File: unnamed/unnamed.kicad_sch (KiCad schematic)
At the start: 131 parts, among them J1 Serial, J2 Serial, J3 Conn_01x01_Female, J4 Conn_01x01_Female, J5 S3B-PH-SM4-TB(LF)(SN), J6 S3B-PH-SM4-TB(LF)(SN), J7 trackball, J8 Conn_01x12_Female, SW1 SW_Push, SW10 SW_Push, SW11 SW_Push, SW12 SW_Push, SW13 SW_Push, SW14 SW_Push, SW15 SW_Push, SW16 SW_Push, SW17 SW_Push, SW18 SW_Push, SW19 SW_Push, SW2 SW_Push, SW20 SW_Push, SW21 SW_Push, SW22 SW_Push, SW23 SW_Push, SW24 SW_Push, SW25 SW_SPST, SW26 SW_SPST, SW27 SW_Push, SW28 SW_Push, SW29 SW_Push, SW3 SW_Push, SW30 SW_Push, SW31 SW_Push, SW32 SW_Push, SW33 SW_Push, SW34 SW_Push, SW35 SW_Push, SW36 SW_Push, SW4 SW_Push, SW5 SW_Push, SW6 SW_Push, SW7 SW_Push, SW8 SW_Push, SW9 SW_Push, U1 eliteC, U2 eliteC

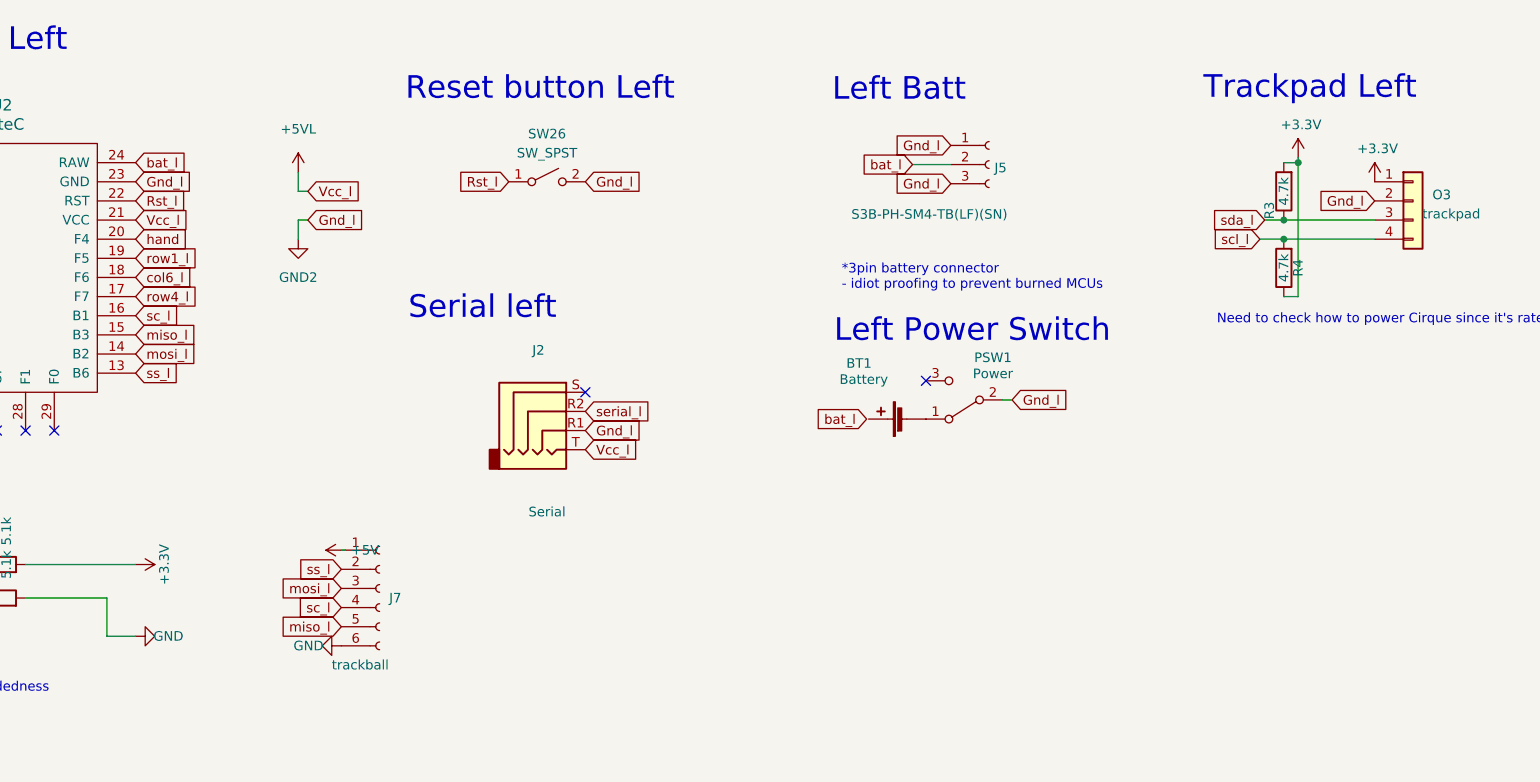
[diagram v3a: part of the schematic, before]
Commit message: trackpad connector
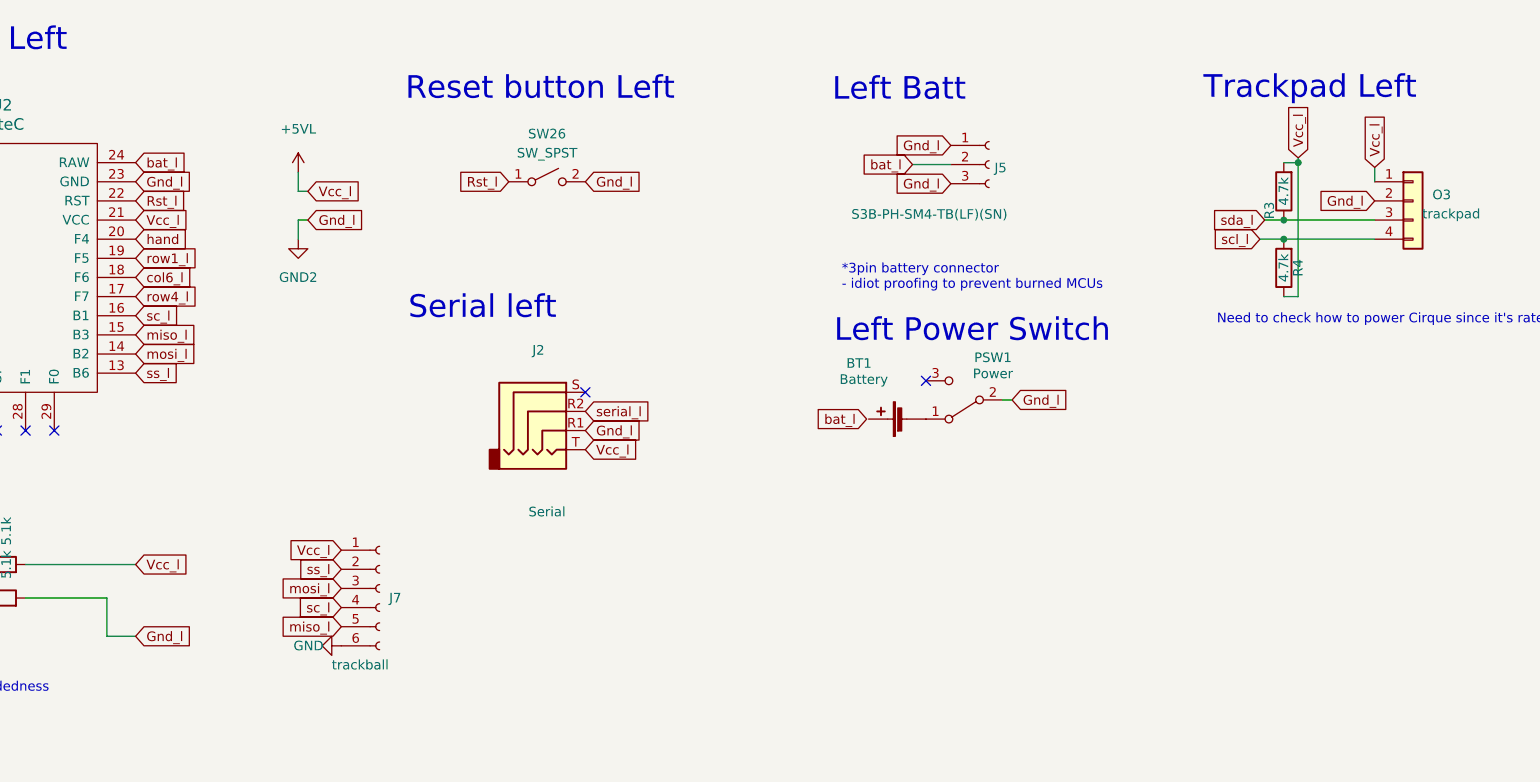
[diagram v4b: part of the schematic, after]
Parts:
- D10, D13, D14, D15, D18, D19, D20, D24, D25, D26, D3, D30, D33, D4, D5, D8, D9: footprint Library:D_1206_handsolder_reversible -> footprints:D_1206_handsolder_reversible
- O3: footprint Connector_PinHeader_2.54mm:PinHeader_1x04_P2.54mm_Vertical -> footprints:PinHeader_1x04_P2.54mm_Vertical
- R7, R8: footprint Resistor_SMD:R_0402_1005Metric -> footprints:D_1206_handsolder
- SW1, SW10, SW11, SW12, SW13, SW14, SW15, SW16, SW17, SW18, SW19, SW2, SW20, SW21, SW22, SW23, SW24, SW25, SW26, SW27, SW28, SW29, SW3, SW30, SW31, SW32, SW33, SW4, SW5, SW6, SW7, SW8, SW9: footprint Library:SW_MX_choc -> footprints:SW_MX_choc
- U2: footprint Library:Elite-C -> footprints:Elite-C
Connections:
- net +3V3: no longer O3.1 (Pin_1), R3.2, R4.1, R7.2
- net +5V: no longer J7.1 (Pin_1)
- net +5VL: now also J7.1 (Pin_1), O3.1 (Pin_1), R3.2, R4.1, R7.2
- net GND: no longer R8.2
- net GND2: now also R8.2

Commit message: cleanup (reversible)
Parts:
- removed BT2: Battery, swoop:Battery_pads_reversible, symbol Device:Battery_Cell
- removed C2: C, symbol Device:C
- removed D35, D36, D40, D41, D45, D46, D50, D51, D55, D56, D57, D61, D62, D63, D65, D66, D68: SK6812MINI, symbol LED:SK6812MINI
- removed D37, D38, D39, D42, D43, D44, D47, D48, D49, D52, D53, D54, D58, D59, D60, D64, D67: D, symbol Device:D
- removed J1: Serial, symbol Connector:AudioJack4
- removed J3: Conn_01x01_Female, symbol Connector:Conn_01x01_Female
- removed J6: S3B-PH-SM4-TB(LF)(SN), Connector_JST:JST_PH_S3B-PH-SM4-TB_1x03-1MP_P2.00mm_Horizontal, symbol Connector:Conn_01x03_Female
- removed J8: Conn_01x12_Female, prettylib:FPC-SMD_FH12-12S-0.5SH-55, symbol Connector:Conn_01x12_Female
- removed O1: OLED, swoop:OLED_jumpers, symbol Connector_Generic:Conn_01x04
- removed PSW2: Power, swoop:Power, symbol Switch:SW_SPDT
- removed R2: R, symbol Device:R
- removed R5, R6: 4.7k, reversible-kicad-footprints:R-0805_2012Metric, symbol Device:R
- removed SW18, SW19, SW20, SW21, SW22, SW23, SW24, SW27, SW28, SW29, SW30, SW31, SW32, SW33: SW_Push, footprints:SW_MX_choc, symbol Switch:SW_Push
- removed SW25: SW_SPST, footprints:SW_MX_choc, symbol Switch:SW_SPST
- removed SW34, SW35, SW36: SW_Push, symbol Switch:SW_Push
- removed U1: eliteC, symbol elite-C:eliteC
- added SW37: SW_SPST, Button_Switch_THT:SW_PUSH_6mm_H9.5mm, symbol Switch:SW_SPST
- J2: footprint (none) -> footprints:Jack_3.5mm_PJ320E_Horizontal_reversible
- SW26: footprint footprints:SW_MX_choc -> Button_Switch_SMD:SW_Push_1P1T_NO_6x6mm_H9.5mm
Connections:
- net col6_l is gone; now on net col5_l: D24.1 (K), D25.1 (K), D26.1 (K), U2.18 (F6)
- net GND2: now also SW37.2 (B)
- net Rst_l: now also SW37.1 (A)
- net col2_l: now also D10.1 (K), D8.1 (K), D9.1 (K), U2.12 (B5); no longer D3.1 (K), D30.1 (K), D4.1 (K), D5.1 (K), U2.11 (B4)
- net col3_l: now also D13.1 (K), D14.1 (K), D15.1 (K), D33.1 (K), U2.10 (E6); no longer D10.1 (K), D8.1 (K), D9.1 (K), U2.12 (B5)
- net col4_l: now also D18.1 (K), D19.1 (K), D20.1 (K), U2.9 (D7); no longer D13.1 (K), D14.1 (K), D15.1 (K), D33.1 (K), U2.10 (E6)
- net col5_l: no longer D18.1 (K), D19.1 (K), D20.1 (K), U2.9 (D7)
- new net col1_l: D3.1 (K), D30.1 (K), D4.1 (K), D5.1 (K), U2.11 (B4)
- no-connect marks 21 -> 7
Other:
- note removed: "MCU Right"
- note removed: "OLED Right"
- note removed: "Reset button Right"
- note removed: "Right"
- note removed: "Right Batt"
- note removed: "Serial right"
- note removed: "Trackpad Right"

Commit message: routing, audio jack, rst button
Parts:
- SW37: footprint Button_Switch_THT:SW_PUSH_6mm_H9.5mm -> Button_Switch_SMD:SW_Push_1P1T_NO_6x6mm_H9.5mm
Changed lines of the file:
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@@
     (property "Reference" "SW37" (id 0) (at 373.38 40.64 0))
     (property "Value" "SW_SPST" (id 1) (at 373.38 43.18 0))
-    (property "Footprint" "Button_Switch_THT:SW_PUSH_6mm_H9.5mm" (id 2) (at 373.38 46.99 0)
+    (property "Footprint" "Button_Switch_SMD:SW_Push_1P1T_NO_6x6mm_H9.5mm" (id 2) (at 373.38 46.99 0)
       (effects (font (size 1.27 1.27)) hide)
     )
@@
     )
     (path "/be3485fb-9d3c-40d5-abfd-0f4dfff6875d"
-      (reference "SW37") (unit 1) (value "SW_SPST") (footprint "Button_Switch_THT:SW_PUSH_6mm_H9.5mm")
+      (reference "SW37") (unit 1) (value "SW_SPST") (footprint "Button_Switch_SMD:SW_Push_1P1T_NO_6x6mm_H9.5mm")
     )
     (path "/be4a846f-e398-4560-93fc-42de85dc5e36"

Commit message: routing
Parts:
- R7, R8: footprint footprints:D_1206_handsolder -> footprints:R_1206_handsolder
- SW26, SW37: footprint Button_Switch_SMD:SW_Push_1P1T_NO_6x6mm_H9.5mm -> footprints:SW_Push_1P1T_NO_6x6mm_H9.5mm
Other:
- moved on the sheet: BT1, J2, J5, J7, O2, O3, PSW1, R3, R4, R7, R8, SW26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

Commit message: holes
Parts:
- added H1, H2, H3, H4: M4, footprints:MountingHole_3mm_Pad_thin, symbol Mechanical:MountingHole_Pad
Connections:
- net GND: now also H1.1, H2.1, H3.1, H4.1
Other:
- note added: "Plate screws"
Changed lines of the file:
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@@
+    (stroke (width 0) (type default) (color 0 0 0 0))
+  )
+  (polyline (pts (xy 315.595 24.13) (xy 315.595 48.895))
     (stroke (width 0) (type default) (color 0 0 0 0))
   )
@@
     (stroke (width 0) (type solid) (color 0 0 0 0))
   )
+  (polyline (pts (xy 288.925 24.13) (xy 315.595 24.13))
+    (stroke (width 0) (type default) (color 0 0 0 0))
+  )
   (wire (pts (xy 120.65 99.06) (xy 128.27 99.06))
     (stroke (width 0) (type solid) (color 0 0 0 0))
@@
     (stroke (width 0) (type default) (color 0 0 0 0))
   )
+  (polyline (pts (xy 315.595 48.895) (xy 288.925 48.895))
+    (stroke (width 0) (type default) (color 0 0 0 0))
+  )
   (wire (pts (xy 66.04 38.1) (xy 67.31 38.1))
+    (stroke (width 0) (type default) (color 0 0 0 0))
+  )
+  (polyline (pts (xy 288.925 24.13) (xy 288.925 48.895))
     (stroke (width 0) (type default) (color 0 0 0 0))
   )
@@
   (text "Handedness" (at 46.355 216.535 0)
     (effects (font (size 1.27 1.27)) (justify left bottom))
+  )
+  (text "Plate screws" (at 302.895 26.67 180)
+    (effects (font (size 1.27 1.27)) (justify right bottom))
   )
   (text "Left" (at 23.495 74.93 90)
@@
     (pin "2")
   )
+  (symbol (lib_id "Mechanical:MountingHole_Pad") (at 299.085 33.655 0) (unit 1)
+    (in_bom yes) (on_board yes)
+    (property "Reference" "H2" (id 0) (at 297.815 28.575 0)
+      (effects (font (size 1.27 1.27)) (justify left))
+    )
+    (property "Value" "M4" (id 1) (at 297.815 45.847 0)
+      (effects (font (size 1.27 1.27)) (justify left))
+    )
+    (property "Footprint" "footprints:MountingHole_3mm_Pad_thin" (id 2) (at 299.085 33.655 0)
+      (effects (font (size 1.27 1.27)) hide)
+    )
+    (property "Datasheet" "~" (id 3) (at 299.085 33.655 0)
+      (effects (font (size 1.27 1.27)) hide)
+    )
+    (pin "1")
+  )
+  (symbol (lib_id "Mechanical:MountingHole_Pad") (at 292.735 33.655 0) (unit 1)
+    (in_bom yes) (on_board yes)
+    (property "Reference" "H1" (id 0) (at 291.465 28.575 0)
+      (effects (font (size 1.27 1.27)) (justify left))
+    )
+    (property "Value" "M4" (id 1) (at 291.465 45.847 0)
+      (effects (font (size 1.27 1.27)) (justify left))
+    )
+    (property "Footprint" "footprints:MountingHole_3mm_Pad_thin" (id 2) (at 292.735 33.655 0)
+      (effects (font (size 1.27 1.27)) hide)
+    )
+    (property "Datasheet" "~" (id 3) (at 292.735 33.655 0)
+      (effects (font (size 1.27 1.27)) hide)
+    )
+    (pin "1")
+  )
   (symbol (lib_id "LED:SK6812MINI") (at 226.06 78.74 0) (unit 1)
     (in_bom yes) (on_board yes)
@@
     (pin "2")
   )
+  (symbol (lib_id "power:GND") (at 305.435 36.195 0) (unit 1)
+    (in_bom yes) (on_board yes)
+    (property "Reference" "#PWR0107" (id 0) (at 305.435 42.545 0)
+      (effects (font (size 1.27 1.27)) hide)
+    )
+    (property "Value" "GND" (id 1) (at 305.279 43.1799 90)
+      (effects (font (size 1.27 1.27)) (justify left))
+    )
+    (property "Footprint" "" (id 2) (at 305.435 36.195 0)
+      (effects (font (size 1.27 1.27)) hide)
+    )
+    (property "Datasheet" "" (id 3) (at 305.435 36.195 0)
+      (effects (font (size 1.27 1.27)) hide)
+    )
+    (pin "1")
+  )
   (symbol (lib_id "power:+5VL") (at 90.17 147.32 0) (unit 1)
     (in_bom yes) (on_board yes) (fields_autoplaced)
@@
     (pin "1")
   )
+  (symbol (lib_id "Mechanical:MountingHole_Pad") (at 305.435 33.655 0) (unit 1)
+    (in_bom yes) (on_board yes)
+    (property "Reference" "H3" (id 0) (at 304.165 28.575 0)
+      (effects (font (size 1.27 1.27)) (justify left))
+    )
+    (property "Value" "M4" (id 1) (at 304.165 45.847 0)
+      (effects (font (size 1.27 1.27)) (justify left))
+    )
+    (property "Footprint" "footprints:MountingHole_3mm_Pad_thin" (id 2) (at 305.435 33.655 0)
+      (effects (font (size 1.27 1.27)) hide)
+    )
+    (property "Datasheet" "~" (id 3) (at 305.435 33.655 0)
+      (effects (font (size 1.27 1.27)) hide)
+    )
+    (pin "1")
+  )
   (symbol (lib_id "Device:D") (at 71.12 48.26 180) (unit 1)
     (in_bom yes) (on_board yes)
@@
     (pin "3")
     (pin "4")
+  )
+  (symbol (lib_id "power:GND") (at 292.735 36.195 0) (unit 1)
+    (in_bom yes) (on_board yes)
+    (property "Reference" "#PWR0104" (id 0) (at 292.735 42.545 0)
+      (effects (font (size 1.27 1.27)) hide)
+    )
+    (property "Value" "GND" (id 1) (at 292.579 43.1799 90)
+      (effects (font (size 1.27 1.27)) (justify left))
+    )
+    (property "Footprint" "" (id 2) (at 292.735 36.195 0)
+      (effects (font (size 1.27 1.27)) hide)
+    )
+    (property "Datasheet" "" (id 3) (at 292.735 36.195 0)
+      (effects (font (size 1.27 1.27)) hide)
+    )
+    (pin "1")
   )
   (symbol (lib_id "Device:D") (at 124.46 38.1 180) (unit 1)
@@
     (pin "1")
     (pin "2")
+  )
+  (symbol (lib_id "power:GND") (at 299.085 36.195 0) (unit 1)
+    (in_bom yes) (on_board yes)
+    (property "Reference" "#PWR0106" (id 0) (at 299.085 42.545 0)
+      (effects (font (size 1.27 1.27)) hide)
+    )
+    (property "Value" "GND" (id 1) (at 298.929 43.1799 90)
+      (effects (font (size 1.27 1.27)) (justify left))
+    )
+    (property "Footprint" "" (id 2) (at 299.085 36.195 0)
+      (effects (font (size 1.27 1.27)) hide)
+    )
+    (property "Datasheet" "" (id 3) (at 299.085 36.195 0)
+      (effects (font (size 1.27 1.27)) hide)
+    )
+    (pin "1")
   )
   (symbol (lib_id "Switch:SW_Push") (at 114.3 58.42 0) (unit 1)
@@
     (pin "4")
   )
+  (symbol (lib_id "Mechanical:MountingHole_Pad") (at 311.785 33.655 0) (unit 1)
+    (in_bom yes) (on_board yes)
+    (property "Reference" "H4" (id 0) (at 310.515 28.575 0)
+      (effects (font (size 1.27 1.27)) (justify left))
+    )
+    (property "Value" "M4" (id 1) (at 310.515 45.847 0)
+      (effects (font (size 1.27 1.27)) (justify left))
+    )
+    (property "Footprint" "footprints:MountingHole_3mm_Pad_thin" (id 2) (at 311.785 33.655 0)
+      (effects (font (size 1.27 1.27)) hide)
+    )
+    (property "Datasheet" "~" (id 3) (at 311.785 33.655 0)
+      (effects (font (size 1.27 1.27)) hide)
+    )
+    (pin "1")
+  )
   (symbol (lib_id "Switch:SW_Push") (at 114.3 48.26 0) (unit 1)
     (in_bom yes) (on_board yes)
@@
     (pin "2")
   )
+  (symbol (lib_id "power:GND") (at 311.785 36.195 0) (unit 1)
+    (in_bom yes) (on_board yes)
+    (property "Reference" "#PWR0103" (id 0) (at 311.785 42.545 0)
+      (effects (font (size 1.27 1.27)) hide)
+    )
+    (property "Value" "GND" (id 1) (at 311.629 43.1799 90)
+      (effects (font (size 1.27 1.27)) (justify left))
+    )
+    (property "Footprint" "" (id 2) (at 311.785 36.195 0)
+      (effects (font (size 1.27 1.27)) hide)
+    )
+    (property "Datasheet" "" (id 3) (at 311.785 36.195 0)
+      (effects (font (size 1.27 1.27)) hide)
+    )
+    (pin "1")
+  )
   (symbol (lib_id "Device:R") (at 220.98 160.02 180) (unit 1)
     (in_bom yes) (on_board yes)
@@
       (reference "#PWR0102") (unit 1) (value "GND2") (footprint "")
     )
+    (path "/fb97fa38-e913-4813-bbb6-ec56f9359020"
+      (reference "#PWR0103") (unit 1) (value "GND") (footprint "")
+    )
+    (path "/9a573a5f-16ed-4bac-a9aa-25b5d86e5dd3"
+      (reference "#PWR0104") (unit 1) (value "GND") (footprint "")
+    )
     (path "/178062be-5523-4d58-b4b2-d19132948441"
       (reference "#PWR0105") (unit 1) (value "GND") (footprint "")
     )
+    (path "/a7be9e53-3c65-4638-b824-3d5371aceb9f"
+      (reference "#PWR0106") (unit 1) (value "GND") (footprint "")
+    )
+    (path "/7ee12246-48f8-49a8-bcd4-e3487c6db589"
+      (reference "#PWR0107") (unit 1) (value "GND") (footprint "")
+    )
     (path "/9e8006cb-49f0-44ed-b39a-9f9d999f305f"
       (reference "BT1") (unit 1) (value "Battery") (footprint "swoop:Battery_pads_reversible")
@@
       (reference "D34") (unit 1) (value "SK6812MINI") (footprint "")
     )
+    (path "/66749c6a-b16f-43be-bab1-76caa7a8a44a"
+      (reference "H1") (unit 1) (value "M4") (footprint "footprints:MountingHole_3mm_Pad_thin")
+    )
+    (path "/64940337-2175-44aa-ab05-e1e92e28a356"
+      (reference "H2") (unit 1) (value "M4") (footprint "footprints:MountingHole_3mm_Pad_thin")
+    )
+    (path "/8f3d2726-b39f-482d-888f-43d8200309de"
+      (reference "H3") (unit 1) (value "M4") (footprint "footprints:MountingHole_3mm_Pad_thin")
+    )
+    (path "/eab541c6-214e-4bdc-a65e-96cf56f5a486"
+      (reference "H4") (unit 1) (value "M4") (footprint "footprints:MountingHole_3mm_Pad_thin")
+    )
     (path "/d91dbeff-81c6-4fb8-bb3a-36a08837981c"
